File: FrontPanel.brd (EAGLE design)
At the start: 45 x 18.5 mm, 11 parts

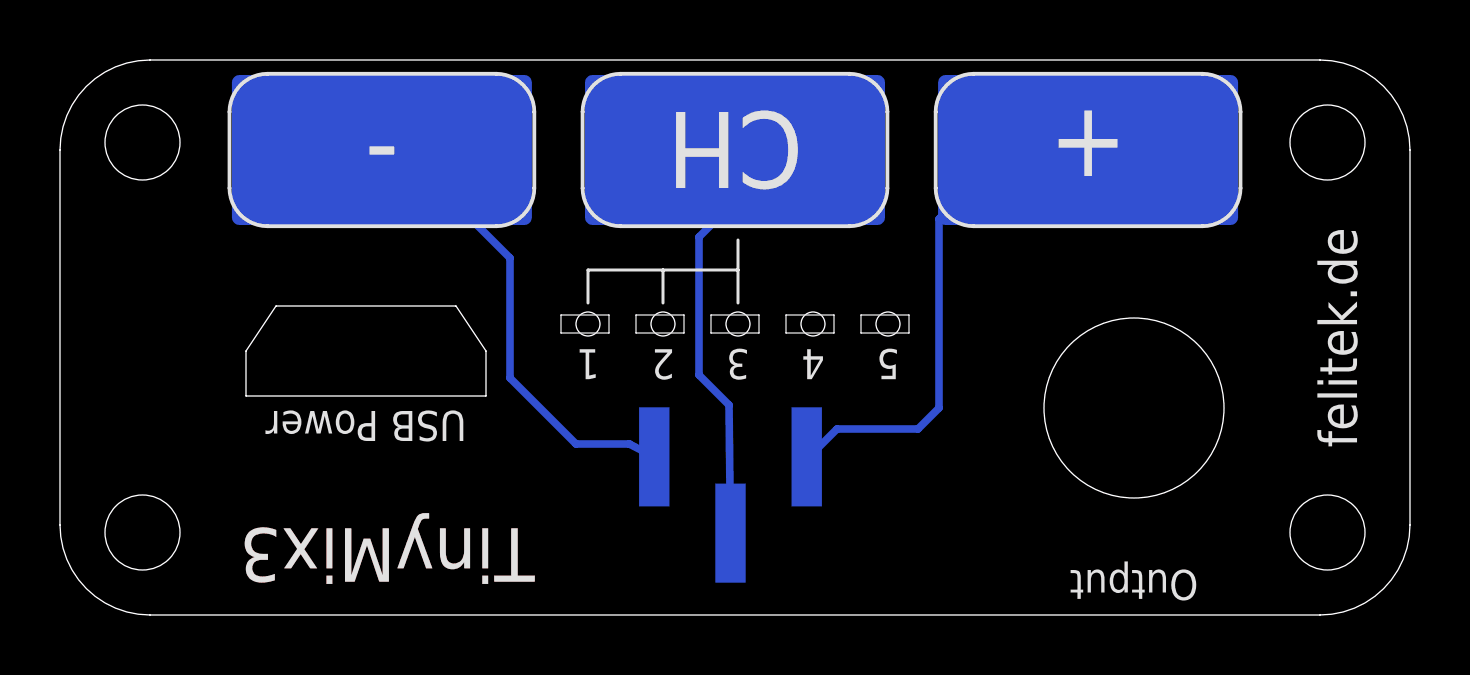
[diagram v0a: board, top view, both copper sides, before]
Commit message: Fixed hole size, use smaller connector for the front panel
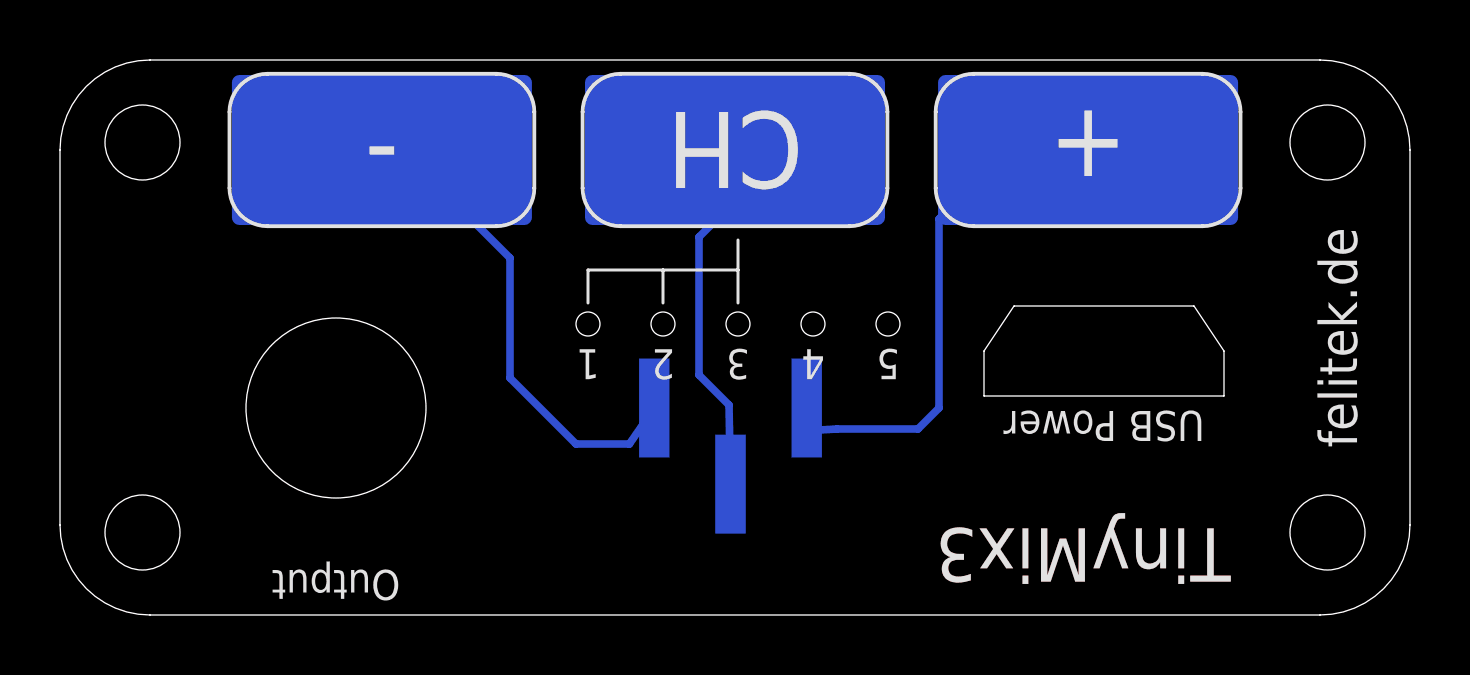
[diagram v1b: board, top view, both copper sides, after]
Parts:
- moved U$1 26.6 mm to (9.20, 6.90)
- moved U$7 24.6 mm to (34.8, 8.80)
- moved JP1 1.63 mm to (22.4, 5.63)
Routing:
- net N$2: track 13.7 -> 12.1 mm
- net N$3: track 15.6 -> 16.1 mm
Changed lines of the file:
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@@
 <?xml version="1.0" encoding="utf-8"?>
 <!DOCTYPE eagle SYSTEM "eagle.dtd">
-<eagle version="6.5.0">
+<eagle version="6.6.0">
 <drawing>
 <settings>
@@
 <layer number="42" name="bRestrict" color="1" fill="10" visible="yes" active="yes"/>
 <layer number="43" name="vRestrict" color="2" fill="10" visible="yes" active="yes"/>
-<layer number="44" name="Drills" color="7" fill="1" visible="yes" active="yes"/>
-<layer number="45" name="Holes" color="7" fill="1" visible="yes" active="yes"/>
+<layer number="44" name="Drills" color="7" fill="1" visible="no" active="yes"/>
+<layer number="45" name="Holes" color="7" fill="1" visible="no" active="yes"/>
 <layer number="46" name="Milling" color="3" fill="1" visible="no" active="yes"/>
 <layer number="47" name="Measures" color="7" fill="1" visible="no" active="yes"/>
@@
 <text x="10.73" y="15.8" size="2.54" layer="25" align="center">-</text>
 <text x="34.27" y="15.9" size="2.54" layer="25" align="center">+</text>
-<text x="10.9" y="2" size="1.778" layer="25" rot="SR180" align="center">TinyMix3</text>
+<text x="34.1" y="2" size="1.778" layer="25" rot="SR180" align="center">TinyMix3</text>
 <text x="42.6" y="9.25" size="1.27" layer="25" rot="R270" align="center">felitek.de</text>
-<text x="35.8" y="1" size="1" layer="25" rot="SR180" align="center">Output</text>
+<text x="9.2" y="1" size="1" layer="25" rot="SR180" align="center">Output</text>
 <text x="17.6" y="8.36" size="1" layer="25" rot="SR180" align="center">1</text>
 <text x="20.1" y="8.36" size="1" layer="25" rot="SR180" align="center">2</text>
@@
 <text x="25.1" y="8.36" size="1" layer="25" rot="SR180" align="center">4</text>
 <text x="27.6" y="8.36" size="1" layer="25" rot="SR180" align="center">5</text>
-<text x="10.2" y="6.3" size="1" layer="25" rot="SR180" align="center">USB Power</text>
+<text x="34.8" y="6.3" size="1" layer="25" rot="SR180" align="center">USB Power</text>
 <wire x1="17.6" y1="10.4" x2="17.6" y2="11.5" width="0.1" layer="25"/>
 <wire x1="17.6" y1="11.5" x2="20.1" y2="11.5" width="0.1" layer="25"/>
@@
 <wire x1="22.6" y1="11.5" x2="22.6" y2="10.4" width="0.1" layer="25"/>
 <wire x1="20.1" y1="10.4" x2="20.1" y2="11.5" width="0.1" layer="25"/>
-<text x="10.9" y="2" size="1.778" layer="1" rot="SR180" align="center">TinyMix3</text>
+<text x="34.1" y="2" size="1.778" layer="1" rot="SR180" align="center">TinyMix3</text>
 </plain>
 <attributes>
@@
 </autorouter>
 <elements>
-<element name="JP1" library="pinhead" package="1X03SMD" value="" x="22.35" y="4" rot="MR0">
-<attribute name="PRICE_100" value="0.536" x="22.35" y="4" size="1.778" layer="28" rot="MR0" display="off"/>
-<attribute name="OC_DIGIKEY" value="S5595-ND" x="22.35" y="4" size="1.778" layer="28" rot="MR0" display="off"/>
+<element name="JP1" library="pinhead" package="1X03SMD" value="" x="22.35" y="5.63" rot="MR0">
+<attribute name="PRICE_100" value="0.536" x="22.35" y="5.63" size="1.778" layer="28" rot="MR0" display="off"/>
+<attribute name="OC_DIGIKEY" value="S5595-ND" x="22.35" y="5.63" size="1.778" layer="28" rot="MR0" display="off"/>
 </element>
-<element name="U$1" library="TinyMix3-FrontPanel" package="FC68125-FP" value="" x="35.8" y="6.9"/>
+<element name="U$1" library="TinyMix3-FrontPanel" package="FC68125-FP" value="" x="9.2" y="6.9"/>
 <element name="U$2" library="TinyMix3-FrontPanel" package="SMDLED_RIGHTANGLE0602" value="" x="27.5" y="9.7" rot="R180"/>
 <element name="U$3" library="TinyMix3-FrontPanel" package="SMDLED_RIGHTANGLE0602" value="" x="25" y="9.7" rot="R180"/>
@@
 <element name="U$5" library="TinyMix3-FrontPanel" package="SMDLED_RIGHTANGLE0602" value="" x="20" y="9.7" rot="R180"/>
 <element name="U$6" library="TinyMix3-FrontPanel" package="SMDLED_RIGHTANGLE0602" value="" x="17.5" y="9.7" rot="R180"/>
-<element name="U$7" library="TinyMix3-FrontPanel" package="SMD-USB-PANEL" value="" x="10.2" y="8.8" rot="R180"/>
+<element name="U$7" library="TinyMix3-FrontPanel" package="SMD-USB-PANEL" value="" x="34.8" y="8.8" rot="R180"/>
 <element name="U$8" library="TinyMix3-FrontPanel" package="TOUCH_FIELD_10X5" value="TOUCHPAD" x="34.27" y="15.5"/>
 <element name="U$9" library="TinyMix3-FrontPanel" package="TOUCH_FIELD_10X5" value="TOUCHPAD" x="22.5" y="15.5"/>
@@
 <contactref element="JP1" pad="1"/>
 <contactref element="U$8" pad="P$1"/>
-<wire x1="24.89" y1="5.27" x2="24.84" y2="5.14" width="0.254" layer="16"/>
-<wire x1="24.84" y1="5.14" x2="25.9" y2="6.2" width="0.254" layer="16"/>
+<wire x1="24.89" y1="6.9" x2="24.84" y2="6.14" width="0.254" layer="16"/>
+<wire x1="24.84" y1="6.14" x2="25.9" y2="6.2" width="0.254" layer="16"/>
 <wire x1="25.9" y1="6.2" x2="28.6" y2="6.2" width="0.254" layer="16"/>
 <wire x1="28.6" y1="6.2" x2="29.3" y2="6.9" width="0.254" layer="16"/>
@@
 <contactref element="JP1" pad="2"/>
 <contactref element="U$9" pad="P$1"/>
-<wire x1="22.35" y1="2.73" x2="22.3" y2="7" width="0.254" layer="16"/>
+<wire x1="22.35" y1="4.36" x2="22.3" y2="7" width="0.254" layer="16"/>
 <wire x1="22.3" y1="7" x2="21.3" y2="8" width="0.254" layer="16"/>
 <wire x1="21.3" y1="8" x2="21.3" y2="12.6" width="0.254" layer="16"/>
@@
 <wire x1="15" y1="7.9" x2="17.2" y2="5.7" width="0.254" layer="16"/>
 <wire x1="17.2" y1="5.7" x2="18.98" y2="5.7" width="0.254" layer="16"/>
-<wire x1="18.98" y1="5.7" x2="19.81" y2="5.27" width="0.254" layer="16"/>
+<wire x1="18.98" y1="5.7" x2="19.81" y2="6.9" width="0.254" layer="16"/>
 </signal>
 </signals>
